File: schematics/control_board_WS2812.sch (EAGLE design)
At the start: 45 parts, among them J1 POWER_JACKPTH, U1 ATMEGA168, Y1 16MHZ

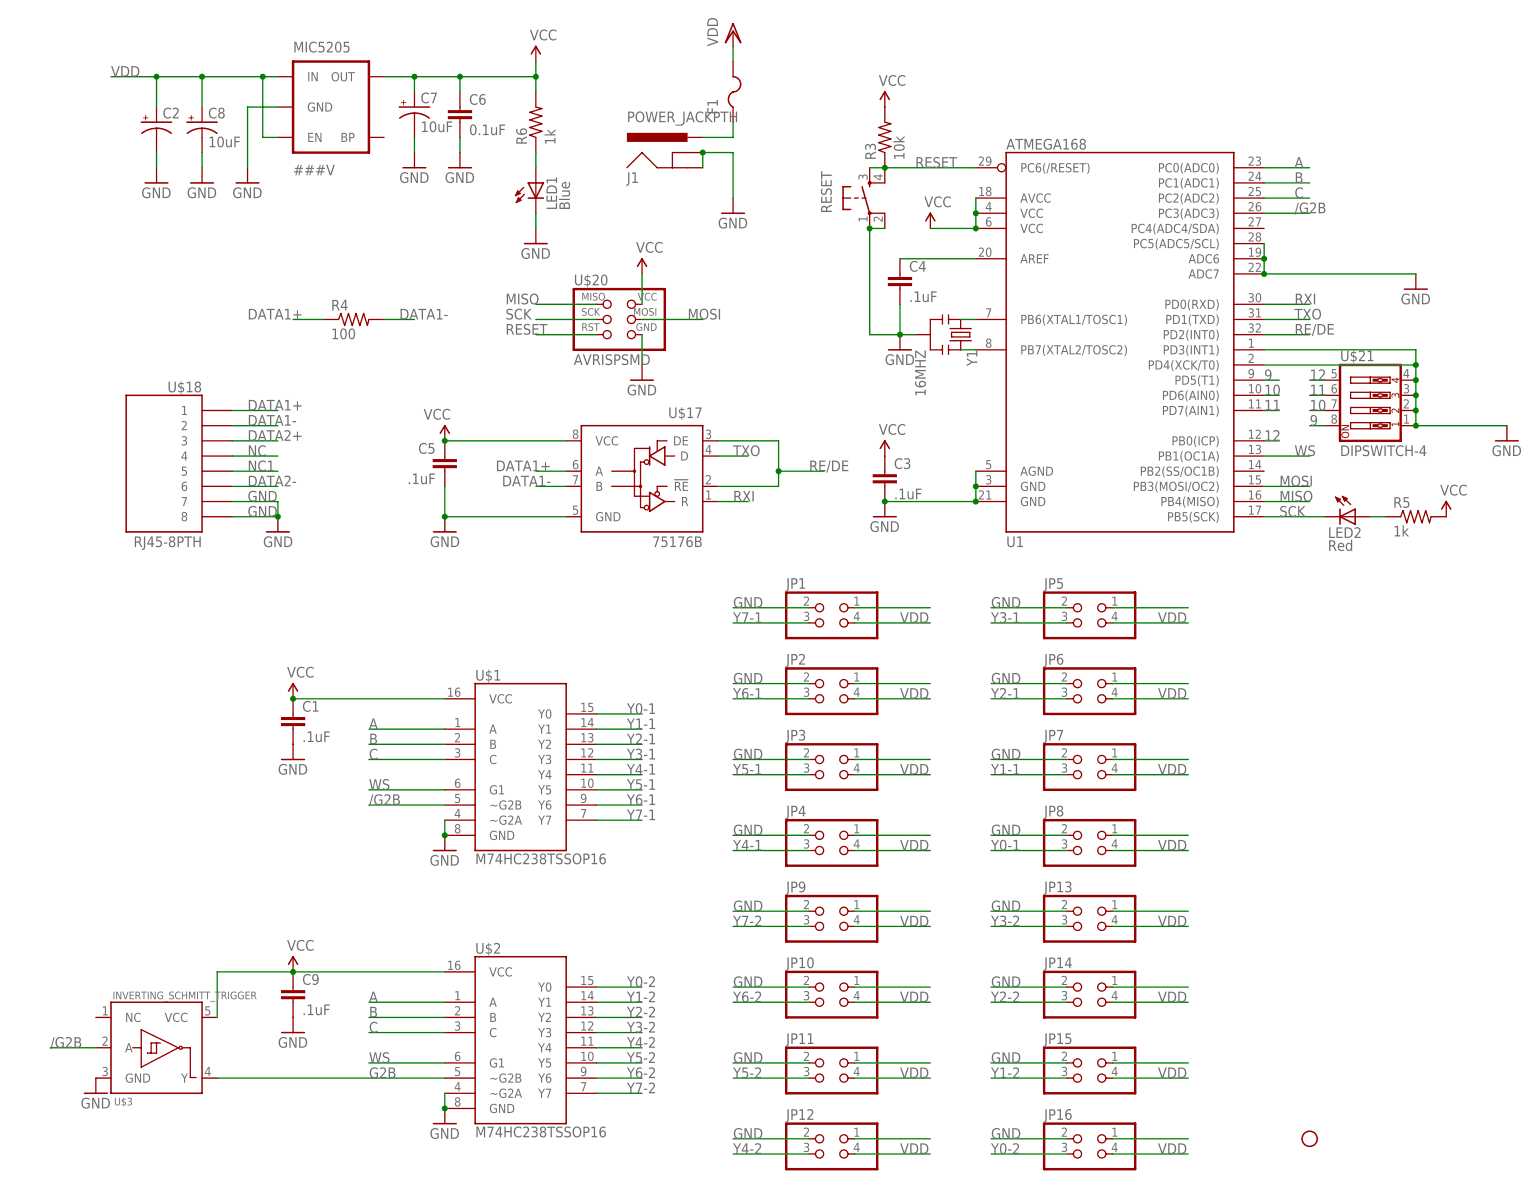
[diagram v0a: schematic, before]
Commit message: changed WS2812 controller to uUSB, minor spacing edits to everything else
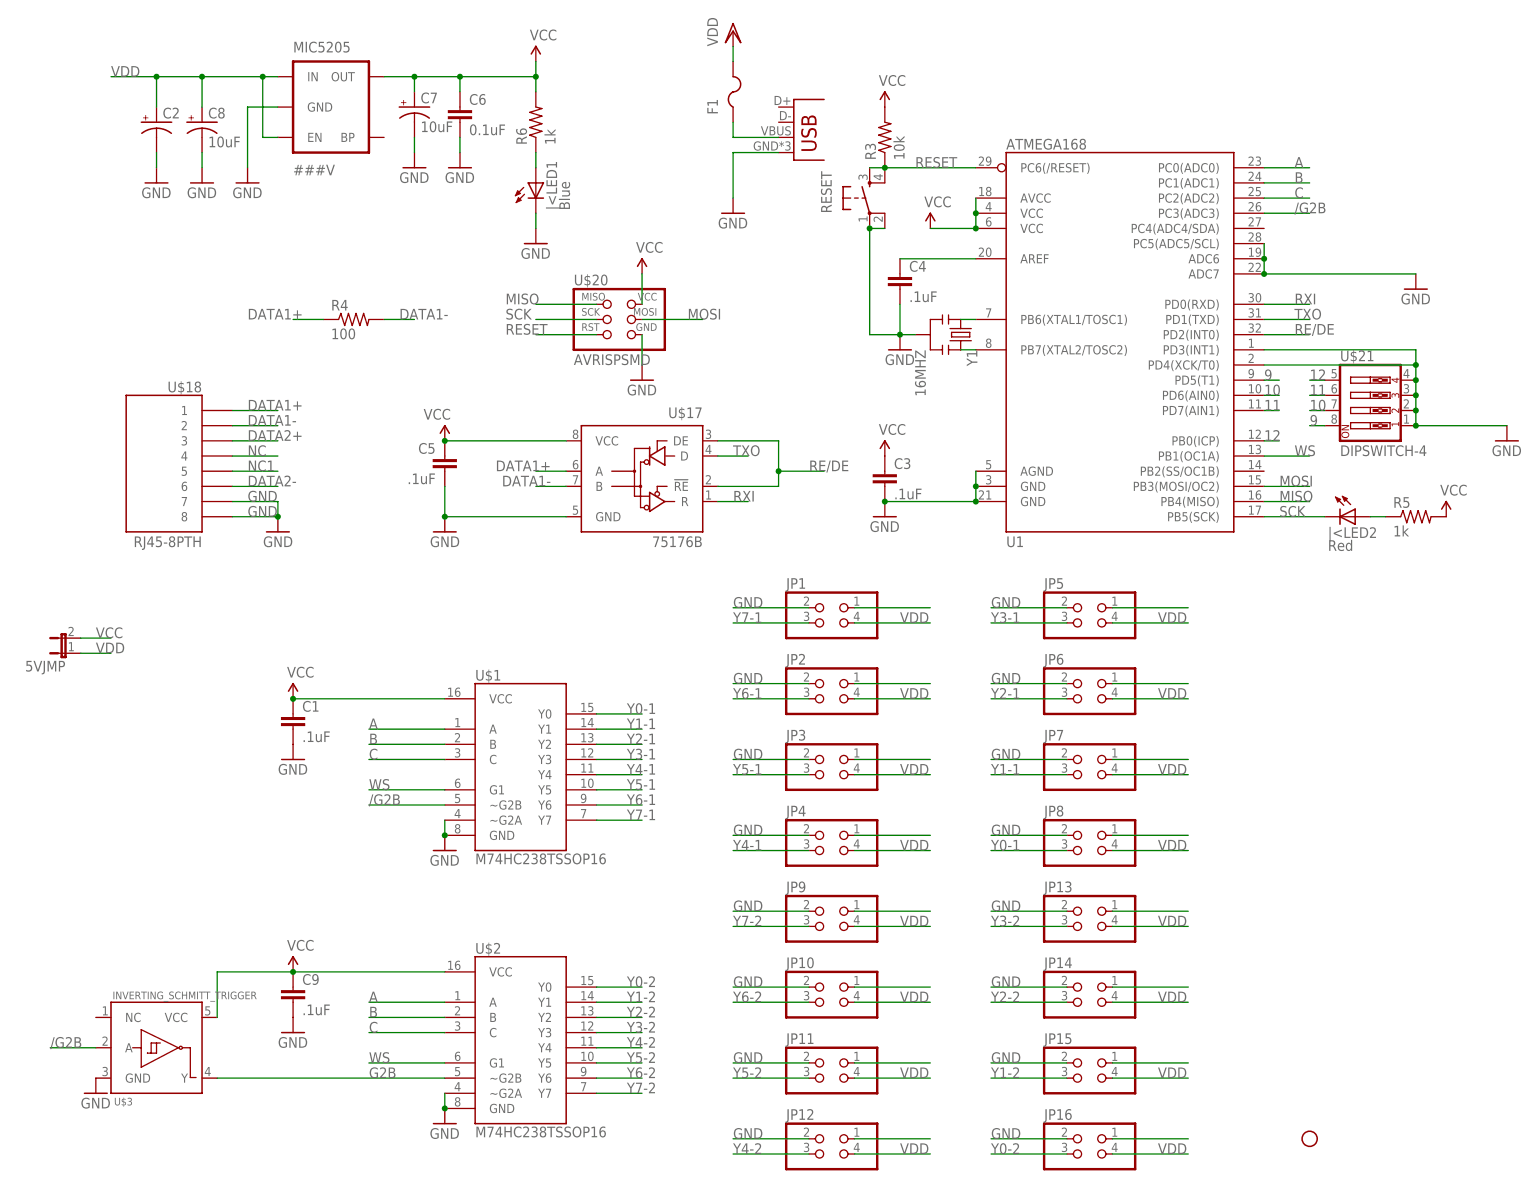
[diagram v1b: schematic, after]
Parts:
- removed J1: POWER_JACKPTH, SparkFun-Connectors:POWER_JACKPTH
- added 5VJMP: (no value), SparkFun-Passives:JUMPER-2SMD-NO
- added JP17: USB-MICROB, SparkFun-Connectors:USB-MICROB
- renumbered LED1 to |<LED1, LED2 to |<LED2
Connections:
- net GND: now also JP17.GND; no longer J1.GND, J1.GNDBREAK
- net N$8: now also JP17.VBUS; no longer J1.PWR
- net VCC: now also 5VJMP.2
- net VDD: now also 5VJMP.1
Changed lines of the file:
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@@
 <part name="GND26" library="SparkFun" deviceset="GND" device=""/>
 <part name="R6" library="SparkFun" deviceset="RESISTOR" device="0402" value="1k"/>
-<part name="LED1" library="SparkFun" deviceset="LED" device="0603" value="Blue"/>
+<part name="|&lt;LED1" library="SparkFun" deviceset="LED" device="0603" value="Blue"/>
 <part name="GND28" library="SparkFun" deviceset="GND" device=""/>
 <part name="MIC5205" library="SparkFun" deviceset="V_REG_LDO" device="SMD" value="###V"/>
@@
 <part name="GND10" library="SparkFun-Aesthetics" deviceset="GND" device=""/>
 <part name="R5" library="SparkFun" deviceset="RESISTOR" device="0402" value="1k"/>
-<part name="LED2" library="SparkFun" deviceset="LED" device="0603" value="Red"/>
+<part name="|&lt;LED2" library="SparkFun" deviceset="LED" device="0603" value="Red"/>
 <part name="SUPPLY8" library="SparkFun-Aesthetics" deviceset="VCC" device=""/>
 <part name="GND12" library="SparkFun-Aesthetics" deviceset="GND" device=""/>
@@
 <part name="JP1" library="pinhead" deviceset="PINHD-2X2" device=""/>
 <part name="C2" library="SparkFun-Capacitors" deviceset="CAP_POL" device="C"/>
-<part name="J1" library="SparkFun-Connectors" deviceset="POWER_JACK" device="PTH"/>
 <part name="U$1" library="SparkFun-DigitalIC" deviceset="M74HC238" device="TSSOP16"/>
 <part name="U$2" library="SparkFun-DigitalIC" deviceset="M74HC238" device="TSSOP16"/>
@@
 <part name="U$3" library="SparkFun-DigitalIC" deviceset="INVERTING_SCHMITT_TRIGGER" device=""/>
 <part name="GND11" library="SparkFun-Aesthetics" deviceset="GND" device=""/>
+<part name="JP17" library="SparkFun-Connectors" deviceset="USB" device="-MICROB"/>
+<part name="5VJMP" library="SparkFun-Passives" deviceset="JUMPER-2" device="SMD-NO"/>
 </parts>
 <sheets>
@@
 <instance part="GND26" gate="1" x="63.5" y="167.64"/>
 <instance part="R6" gate="G$1" x="76.2" y="175.26" rot="R90"/>
-<instance part="LED1" gate="G$1" x="76.2" y="165.1"/>
+<instance part="|&lt;LED1" gate="G$1" x="76.2" y="165.1"/>
 <instance part="GND28" gate="1" x="76.2" y="154.94"/>
 <instance part="MIC5205" gate="G$1" x="43.18" y="177.8"/>
@@
 <instance part="GND10" gate="1" x="238.76" y="121.92"/>
 <instance part="R5" gate="G$1" x="223.52" y="109.22"/>
-<instance part="LED2" gate="G$1" x="213.36" y="109.22" rot="R270"/>
+<instance part="|&lt;LED2" gate="G$1" x="213.36" y="109.22" rot="R270"/>
 <instance part="SUPPLY8" gate="1" x="228.6" y="109.22"/>
 <instance part="GND12" gate="1" x="223.52" y="147.32"/>
@@
 <instance part="JP1" gate="A" x="127" y="91.44"/>
 <instance part="C2" gate="G$1" x="12.7" y="175.26"/>
-<instance part="J1" gate="G$1" x="101.6" y="165.1"/>
 <instance part="U$1" gate="G$1" x="73.66" y="66.04"/>
 <instance part="U$2" gate="G$1" x="73.66" y="20.32"/>
@@
 <instance part="U$3" gate="G$1" x="12.7" y="20.32"/>
 <instance part="GND11" gate="1" x="2.54" y="12.7"/>
+<instance part="JP17" gate="G$1" x="119.38" y="170.18"/>
+<instance part="5VJMP" gate="A" x="-2.54" y="86.36" rot="R90"/>
 </instances>
 <busses>
@@
 <segment>
 <wire x1="76.2" y1="157.48" x2="76.2" y2="160.02" width="0.1524" layer="91"/>
-<pinref part="LED1" gate="G$1" pin="C"/>
+<pinref part="|&lt;LED1" gate="G$1" pin="C"/>
 <pinref part="GND28" gate="1" pin="GND"/>
 </segment>
@@
 <segment>
 <wire x1="109.22" y1="170.18" x2="109.22" y2="162.56" width="0.1524" layer="91"/>
-<pinref part="J1" gate="G$1" pin="GNDBREAK"/>
-<pinref part="J1" gate="G$1" pin="GND"/>
-<wire x1="104.14" y1="170.18" x2="104.14" y2="167.64" width="0.1524" layer="91"/>
-<wire x1="109.22" y1="170.18" x2="104.14" y2="170.18" width="0.1524" layer="91"/>
-<junction x="104.14" y="170.18"/>
 <pinref part="GND1" gate="1" pin="GND"/>
+<pinref part="JP17" gate="G$1" pin="GND"/>
+<wire x1="116.84" y1="170.18" x2="109.22" y2="170.18" width="0.1524" layer="91"/>
 </segment>
 <segment>
@@
 <wire x1="22.86" y1="33.02" x2="22.86" y2="25.4" width="0.1524" layer="91"/>
 </segment>
+<segment>
+<pinref part="5VJMP" gate="A" pin="2"/>
+<wire x1="0" y1="88.9" x2="5.08" y2="88.9" width="0.1524" layer="91"/>
+<label x="2.54" y="88.9" size="1.778" layer="95"/>
+</segment>
 </net>
 <net name="MOSI" class="0">
@@
 <wire x1="198.12" y1="109.22" x2="208.28" y2="109.22" width="0.1524" layer="91"/>
 <label x="200.66" y="109.22" size="1.778" layer="95"/>
-<pinref part="LED2" gate="G$1" pin="C"/>
+<pinref part="|&lt;LED2" gate="G$1" pin="C"/>
 </segment>
 </net>
@@
 <label x="180.34" y="2.54" size="1.778" layer="95"/>
 </segment>
+<segment>
+<pinref part="5VJMP" gate="A" pin="1"/>
+<wire x1="0" y1="86.36" x2="5.08" y2="86.36" width="0.1524" layer="91"/>
+<label x="2.54" y="86.36" size="1.778" layer="95"/>
+</segment>
 </net>
 <net name="DATA1+" class="0">
@@
 <wire x1="76.2" y1="167.64" x2="76.2" y2="170.18" width="0.1524" layer="91"/>
 <pinref part="R6" gate="G$1" pin="1"/>
-<pinref part="LED1" gate="G$1" pin="A"/>
+<pinref part="|&lt;LED1" gate="G$1" pin="A"/>
 </segment>
 </net>
@@
 <wire x1="215.9" y1="109.22" x2="218.44" y2="109.22" width="0.1524" layer="91"/>
 <pinref part="R5" gate="G$1" pin="1"/>
-<pinref part="LED2" gate="G$1" pin="A"/>
+<pinref part="|&lt;LED2" gate="G$1" pin="A"/>
 </segment>
 </net>
@@
 <pinref part="F1" gate="G$1" pin="1"/>
 <wire x1="109.22" y1="175.26" x2="109.22" y2="172.72" width="0.1524" layer="91"/>
-<pinref part="J1" gate="G$1" pin="PWR"/>
-<wire x1="104.14" y1="172.72" x2="109.22" y2="172.72" width="0.1524" layer="91"/>
-</segment>
-</net>
+<pinref part="JP17" gate="G$1" pin="VBUS"/>
+<wire x1="116.84" y1="172.72" x2="109.22" y2="172.72" width="0.1524" layer="91"/>
+</segment>
+</net>
